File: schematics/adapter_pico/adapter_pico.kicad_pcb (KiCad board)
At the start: 2 copper layers, 32 x 53.6 mm, 2 parts, among them J1 Conn_02x20_Odd_Even, U2 Pico

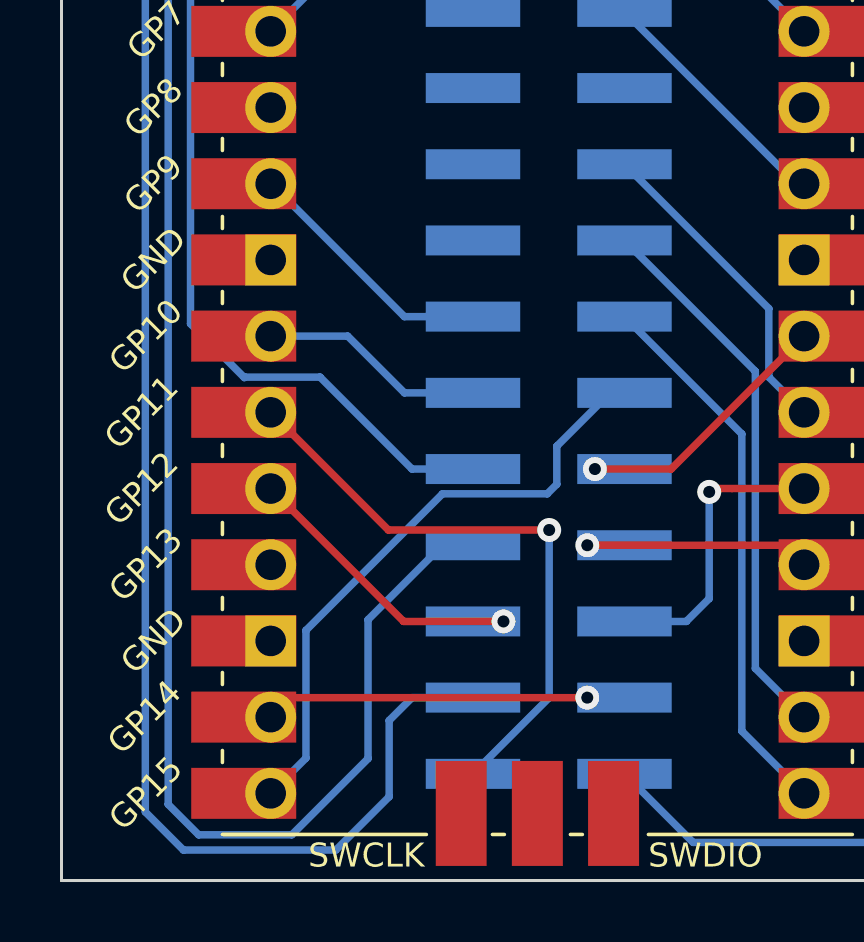
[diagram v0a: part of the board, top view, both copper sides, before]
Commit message: correct codec sdin and sdout directions
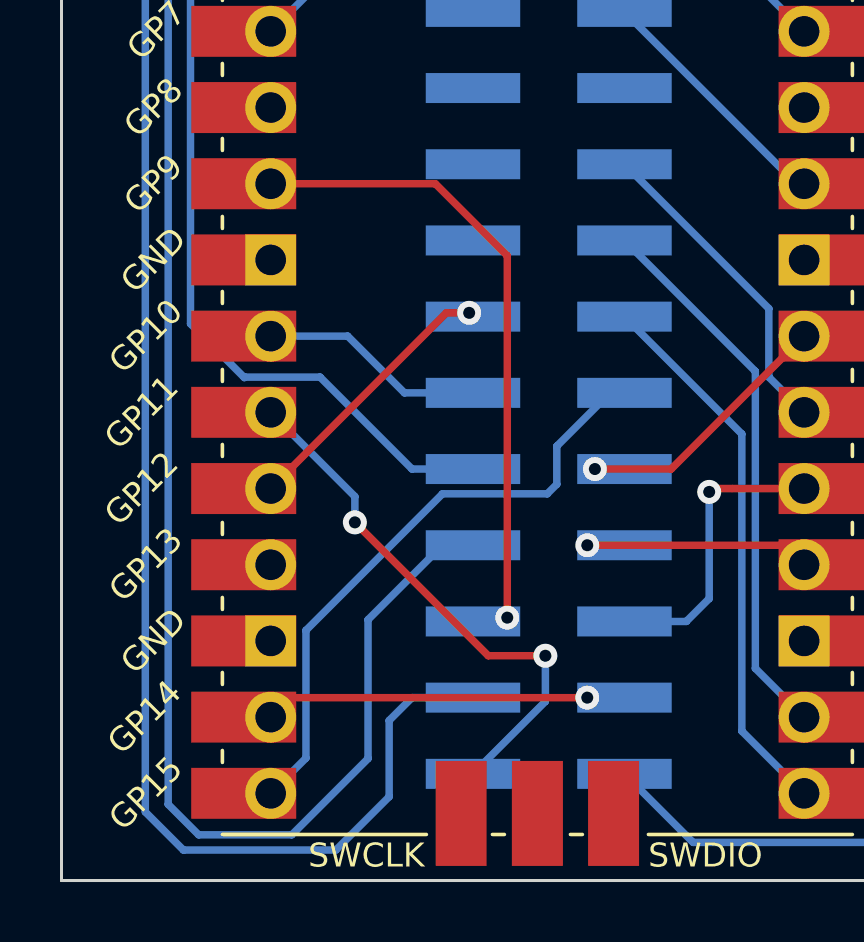
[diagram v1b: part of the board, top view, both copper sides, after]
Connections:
- J1 pad 20: unconnected-(J1-Pin_20-Pad20) -> GND
- J1 pad 39: GND -> unconnected-(J1-Pin_39-Pad39)
- U2 pad 12: Net-(J1-Pin_13) -> Net-(J1-Pin_5)
- U2 pad 16: Net-(J1-Pin_5) -> Net-(J1-Pin_13)
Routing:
- net Net-(J1-Pin_5): track 9.59 -> 21.0 mm
- net Net-(J1-Pin_1): track 20.1 -> 18.0 mm, vias 1 -> 2
- net Net-(J1-Pin_13): track 8.58 -> 9.04 mm, vias 0 -> 1
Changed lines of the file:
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@@
   (net 18 "Net-(J1-Pin_18)")
   (net 19 "GND")
-  (net 20 "unconnected-(J1-Pin_20-Pad20)")
+  (net 20 "unconnected-(J1-Pin_39-Pad39)")
   (net 21 "unconnected-(J1-Pin_21-Pad21)")
   (net 22 "Net-(J1-Pin_22)")
@@
       (net 43 "unconnected-(U2-GPIO8-Pad11)") (pinfunction "GPIO8") (pintype "bidirectional+no_connect"))
     (pad "12" thru_hole oval (at -8.89 3.81) (size 1.7 1.7) (drill 1.02) (layers "*.Cu" "*.Mask")
-      (net 13 "Net-(J1-Pin_13)") (pinfunction "GPIO9") (pintype "bidirectional"))
+      (net 5 "Net-(J1-Pin_5)") (pinfunction "GPIO9") (pintype "bidirectional"))
     (pad "12" smd rect (at -8.89 3.81) (size 3.5 1.7) (drill (offset -0.9 0)) (layers "F.Cu" "F.Mask")
-      (net 13 "Net-(J1-Pin_13)") (pinfunction "GPIO9") (pintype "bidirectional"))
+      (net 5 "Net-(J1-Pin_5)") (pinfunction "GPIO9") (pintype "bidirectional"))
     (pad "13" thru_hole rect (at -8.89 6.35) (size 1.7 1.7) (drill 1.02) (layers "*.Cu" "*.Mask")
       (net 19 "GND") (pinfunction "GND") (pintype "power_in"))
@@
       (net 1 "Net-(J1-Pin_1)") (pinfunction "GPIO11") (pintype "bidirectional"))
     (pad "16" thru_hole oval (at -8.89 13.97) (size 1.7 1.7) (drill 1.02) (layers "*.Cu" "*.Mask")
-      (net 5 "Net-(J1-Pin_5)") (pinfunction "GPIO12") (pintype "bidirectional"))
+      (net 13 "Net-(J1-Pin_13)") (pinfunction "GPIO12") (pintype "bidirectional"))
     (pad "16" smd rect (at -8.89 13.97) (size 3.5 1.7) (drill (offset -0.9 0)) (layers "F.Cu" "F.Mask")
-      (net 5 "Net-(J1-Pin_5)") (pinfunction "GPIO12") (pintype "bidirectional"))
+      (net 13 "Net-(J1-Pin_13)") (pinfunction "GPIO12") (pintype "bidirectional"))
     (pad "17" thru_hole oval (at -8.89 16.51) (size 1.7 1.7) (drill 1.02) (layers "*.Cu" "*.Mask")
       (net 44 "unconnected-(U2-GPIO13-Pad17)") (pinfunction "GPIO13") (pintype "bidirectional+no_connect"))
@@
       (net 19 "GND") (pinfunction "Pin_19") (pintype "passive"))
     (pad "20" smd rect (at 2.525 1.27) (size 3.15 1) (layers "B.Cu" "B.Paste" "B.Mask")
-      (net 20 "unconnected-(J1-Pin_20-Pad20)") (pinfunction "Pin_20") (pintype "passive+no_connect"))
+      (net 19 "GND") (pinfunction "Pin_20") (pintype "passive"))
     (pad "21" smd rect (at -2.525 -1.27) (size 3.15 1) (layers "B.Cu" "B.Paste" "B.Mask")
       (net 21 "unconnected-(J1-Pin_21-Pad21)") (pinfunction "Pin_21") (pintype "passive+no_connect"))
@@
       (net 38 "unconnected-(J1-Pin_38-Pad38)") (pinfunction "Pin_38") (pintype "passive+no_connect"))
     (pad "39" smd rect (at -2.525 -24.13) (size 3.15 1) (layers "B.Cu" "B.Paste" "B.Mask")
-      (net 19 "GND") (pinfunction "Pin_39") (pintype "passive"))
+      (net 20 "unconnected-(J1-Pin_39-Pad39)") (pinfunction "Pin_39") (pintype "passive+no_connect"))
     (pad "40" smd rect (at 2.525 -24.13) (size 3.15 1) (layers "B.Cu" "B.Paste" "B.Mask")
       (net 39 "unconnected-(J1-Pin_40-Pad40)") (pinfunction "Pin_40") (pintype "passive+no_connect"))
@@
   (gr_rect (start 153.416 58.674) (end 185.42 112.268)
     (stroke (width 0.1) (type default)) (fill none) (layer "Edge.Cuts"))
-  (segment (start 169.672 100.584) (end 164.311 100.584) (width 0.25) (layer "F.Cu") (net 1))
-  (segment (start 164.311 100.584) (end 160.389 96.662) (width 0.25) (layer "F.Cu") (net 1))
-  (via (at 169.672 100.584) (size 0.8) (drill 0.4) (layers "F.Cu" "B.Cu") (net 1))
-  (segment (start 167.132 108.712) (end 169.672 106.172) (width 0.25) (layer "B.Cu") (net 1))
-  (segment (start 169.672 106.172) (end 169.672 100.584) (width 0.25) (layer "B.Cu") (net 1))
+  (segment (start 167.64 104.775) (end 169.545 104.775) (width 0.25) (layer "F.Cu") (net 1))
+  (segment (start 163.195 100.33) (end 167.64 104.775) (width 0.25) (layer "F.Cu") (net 1))
+  (via (at 163.195 100.33) (size 0.8) (drill 0.4) (layers "F.Cu" "B.Cu") (net 1))
+  (via (at 169.545 104.775) (size 0.8) (drill 0.4) (layers "F.Cu" "B.Cu") (net 1))
+  (segment (start 163.195 99.468) (end 163.195 100.33) (width 0.25) (layer "B.Cu") (net 1))
+  (segment (start 169.545 104.775) (end 169.545 106.299) (width 0.25) (layer "B.Cu") (net 1))
+  (segment (start 160.389 96.662) (end 163.195 99.468) (width 0.25) (layer "B.Cu") (net 1))
+  (segment (start 169.545 106.299) (end 167.132 108.712) (width 0.25) (layer "B.Cu") (net 1))
   (segment (start 181.864 109.728) (end 180.594 110.998) (width 0.25) (layer "B.Cu") (net 2))
   (segment (start 180.594 110.998) (end 174.468 110.998) (width 0.25) (layer "B.Cu") (net 2))
@@
   (segment (start 161.039 106.172) (end 160.389 106.822) (width 0.25) (layer "F.Cu") (net 4))
   (via (at 170.942 106.172) (size 0.8) (drill 0.4) (layers "F.Cu" "B.Cu") (net 4))
-  (segment (start 164.819 103.632) (end 168.148 103.632) (width 0.25) (layer "F.Cu") (net 5))
-  (segment (start 160.389 99.202) (end 164.819 103.632) (width 0.25) (layer "F.Cu") (net 5))
-  (via (at 168.148 103.632) (size 0.8) (drill 0.4) (layers "F.Cu" "B.Cu") (net 5))
+  (segment (start 168.275 103.505) (end 168.275 91.44) (width 0.25) (layer "F.Cu") (net 5))
+  (segment (start 165.877 89.042) (end 160.389 89.042) (width 0.25) (layer "F.Cu") (net 5))
+  (segment (start 168.275 91.44) (end 165.877 89.042) (width 0.25) (layer "F.Cu") (net 5))
+  (via (at 168.275 103.505) (size 0.8) (drill 0.4) (layers "F.Cu" "B.Cu") (net 5))
+  (segment (start 160.389 89.042) (end 160.416 89.042) (width 0.25) (layer "B.Cu") (net 5))
   (segment (start 175.768 99.202) (end 175.118 99.202) (width 0.25) (layer "F.Cu") (net 6))
   (segment (start 175.118 99.202) (end 175.006 99.314) (width 0.25) (layer "F.Cu") (net 6))
@@
   (segment (start 161.564 103.929) (end 166.116 99.377) (width 0.25) (layer "B.Cu") (net 12))
   (segment (start 160.389 109.362) (end 161.564 108.187) (width 0.25) (layer "B.Cu") (net 12))
-  (segment (start 160.389 89.042) (end 160.416 89.042) (width 0.25) (layer "B.Cu") (net 13))
-  (segment (start 164.846 93.472) (end 167.132 93.472) (width 0.25) (layer "B.Cu") (net 13))
-  (segment (start 160.416 89.042) (end 164.846 93.472) (width 0.25) (layer "B.Cu") (net 13))
+  (segment (start 166.246 93.345) (end 160.389 99.202) (width 0.25) (layer "F.Cu") (net 13))
+  (segment (start 167.005 93.345) (end 166.246 93.345) (width 0.25) (layer "F.Cu") (net 13))
+  (via (at 167.005 93.345) (size 0.8) (drill 0.4) (layers "F.Cu" "B.Cu") (net 13))
   (segment (start 176.094 107.287) (end 178.169 109.362) (width 0.25) (layer "B.Cu") (net 14))
   (segment (start 172.182 93.472) (end 176.094 97.384) (width 0.25) (layer "B.Cu") (net 14))

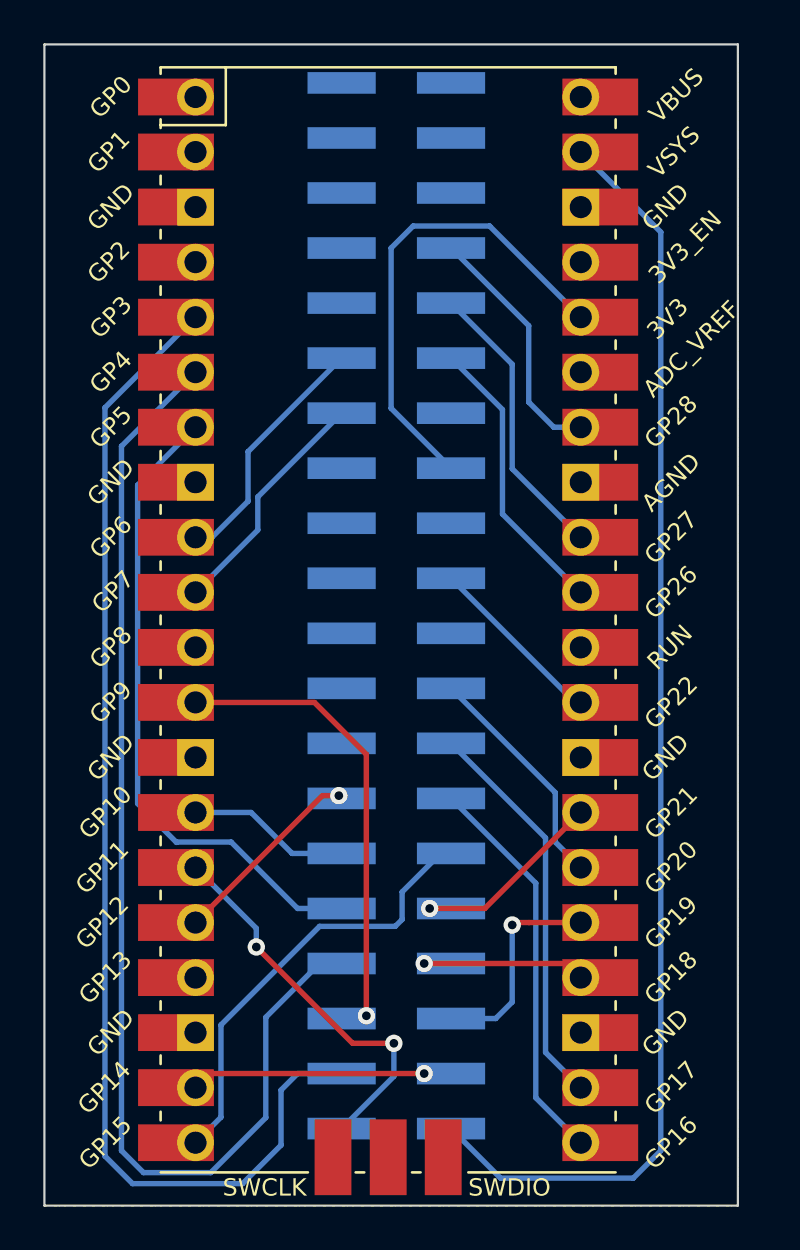
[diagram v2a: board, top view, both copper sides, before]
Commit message: avr flasher: schematic changes
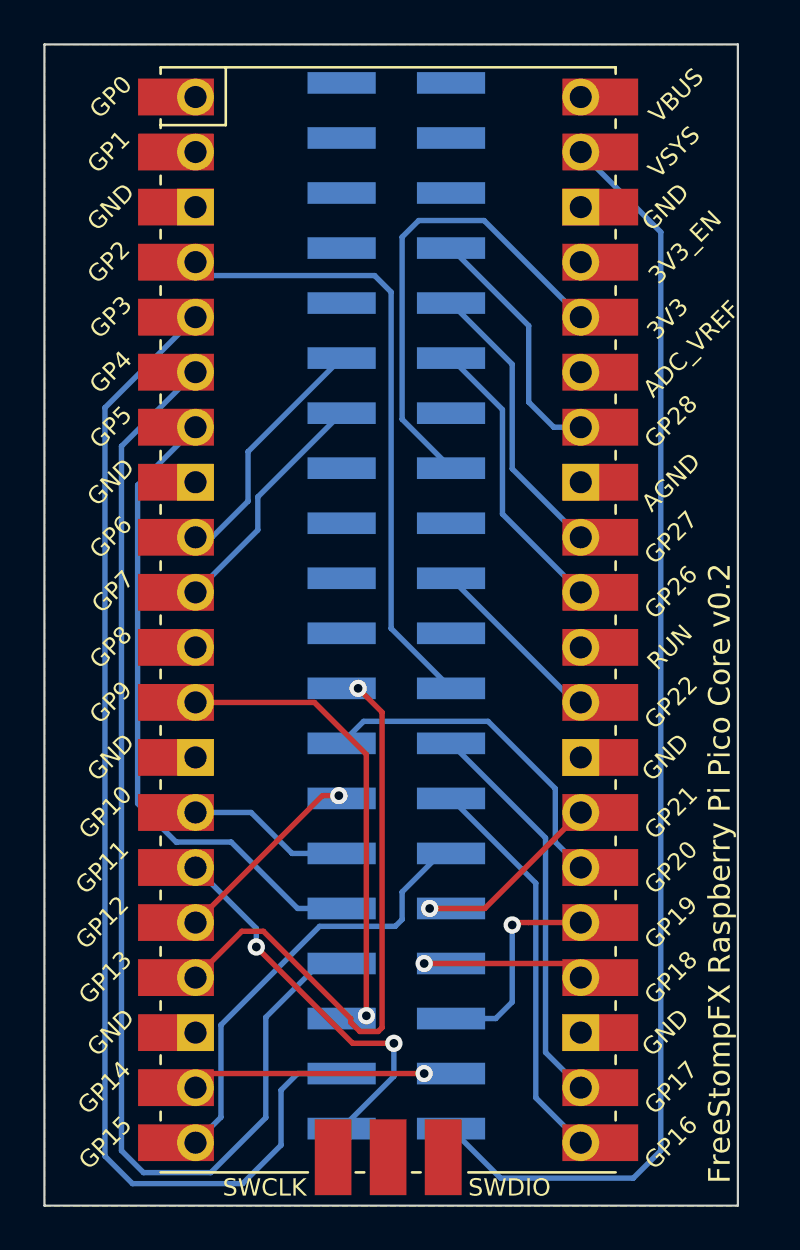
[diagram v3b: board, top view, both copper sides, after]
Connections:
- J1 pad 15: unconnected-(J1-Pin_15-Pad15) -> Net-(J1-Pin_15)
- J1 pad 17: unconnected-(J1-Pin_17-Pad17) -> Net-(J1-Pin_17)
- U2 pad 17: unconnected-(U2-GPIO13-Pad17) -> Net-(J1-Pin_17)
- U2 pad 26: Net-(J1-Pin_18) -> Net-(J1-Pin_15)
- U2 pad 4: unconnected-(U2-GPIO2-Pad4) -> Net-(J1-Pin_18)
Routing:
- net Net-(J1-Pin_17): track 0.00 -> 27.7 mm, vias 0 -> 1
- net Net-(J1-Pin_18): track 10.7 -> 29.0 mm
- net Net-(J1-Pin_15): track 0.00 -> 16.8 mm
- net unconnected-(J1-Pin_15-Pad15): track 1.08 -> 0.00 mm
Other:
- board text added: "FreeStompFX Raspberry Pi Pico Core v0.2"
